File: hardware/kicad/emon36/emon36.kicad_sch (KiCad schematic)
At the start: 80 parts, among them J1 Barrel_Jack, J17 Conn_02x03_Odd_Even, J37 USB_B_Micro, J4 Barrel_Jack, SW2 SW_MEC_5E, SW3 SW_MEC_5E, SW4 SW_MEC_5E, U1 ESP32-C3-WROOM-02-N4, U11 PL133-97QC, U12 PEC12R-4117F-S0012, U3 16.384MHz, U8 TPS5403

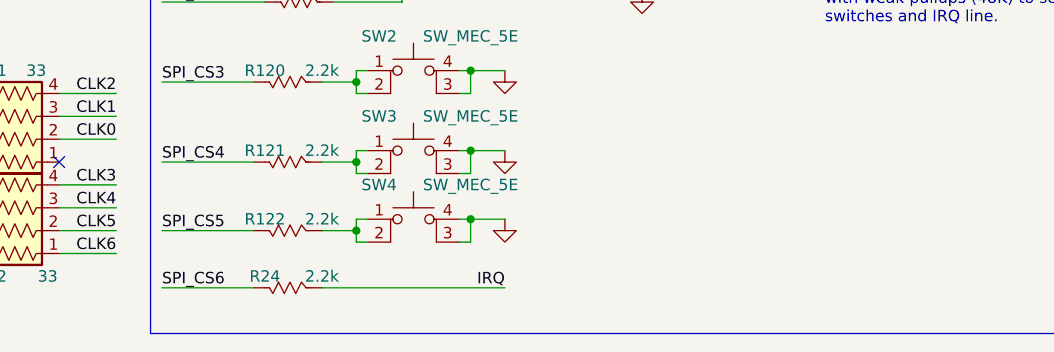
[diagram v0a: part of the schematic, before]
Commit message: Added an optional pullup resistor in case the internal one is not strong enough to boas all the IRQ diodes.
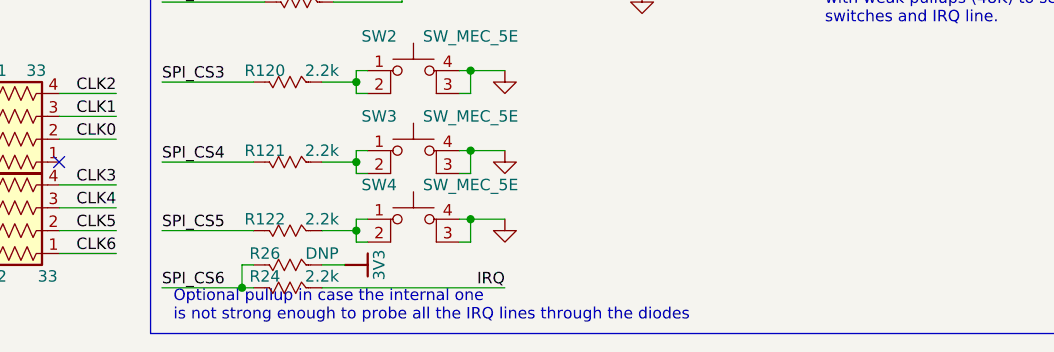
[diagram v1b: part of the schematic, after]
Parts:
- added R26: DNP, Resistor_SMD:R_0603_1608Metric, symbol emon36:R_US
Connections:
- net 3V3: now also R26.2
- net SPI_CS6: now also R26.1
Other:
- note added: "Optional pullup in case the internal one is not strong enough to probe all the IRQ lines through the diodes"
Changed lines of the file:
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@@
   (junction (at 143.51 31.75) (diameter 0) (color 0 0 0 0)
   )
+  (junction (at 119.38 199.39) (diameter 0) (color 0 0 0 0)
+  )
   (junction (at 25.4 123.19) (diameter 0) (color 0 0 0 0)
   )
@@
     (stroke (width 0) (type default) (color 0 0 0 0))
   )
-  (wire (pts (xy 110.49 199.39) (xy 120.65 199.39))
+  (wire (pts (xy 110.49 199.39) (xy 119.38 199.39))
     (stroke (width 0) (type default) (color 0 0 0 0))
   )
@@
     (stroke (width 0) (type default) (color 0 0 0 0))
   )
+  (wire (pts (xy 119.38 199.39) (xy 120.65 199.39))
+    (stroke (width 0) (type default) (color 0 0 0 0))
+  )
   (wire (pts (xy 21.59 83.82) (xy 38.1 83.82))
     (stroke (width 0) (type default) (color 0 0 0 0))
@@
     (stroke (width 0) (type default) (color 0 0 0 0))
   )
+  (wire (pts (xy 119.38 196.85) (xy 119.38 199.39))
+    (stroke (width 0) (type default) (color 0 0 0 0))
+  )
   (wire (pts (xy 213.36 20.32) (xy 213.36 29.21))
     (stroke (width 0) (type default) (color 0 0 0 0))
@@
     (stroke (width 0) (type default) (color 0 0 0 0))
   )
+  (wire (pts (xy 120.65 196.85) (xy 119.38 196.85))
+    (stroke (width 0) (type default) (color 0 0 0 0))
+  )
   (wire (pts (xy 205.74 120.65) (xy 205.74 127))
     (stroke (width 0) (type default) (color 0 0 0 0))
@@
     (stroke (width 0) (type default) (color 0 0 0 0))
   )
+  (wire (pts (xy 128.27 196.85) (xy 130.81 196.85))
+    (stroke (width 0) (type default) (color 0 0 0 0))
+  )
   (wire (pts (xy 143.51 175.26) (xy 144.78 175.26))
     (stroke (width 0) (type default) (color 0 0 0 0))
@@
     (effects (font (size 1.27 1.27)) (justify left bottom))
   )
+  (text "Optional pullup in case the internal one\nis not strong enough to probe all the IRQ lines through the diodes"
+    (at 111.76 203.2 0)
+    (effects (font (size 1.27 1.27)) (justify left bottom))
+  )
   (text "OLED Color Display\n96x64 pixels, 16-bit color\n3.3V supply, SPI interface\n"
     (at 104.14 49.53 0)
@@
     (pin "C")
   )
+  (symbol (lib_id "Top-altium-import:3V3") (at 130.81 196.85 90) (unit 1)
+    (in_bom yes) (on_board yes)
+    (property "Reference" "#PWR0111" (id 0) (at 130.81 196.85 0)
+      (effects (font (size 1.27 1.27)) hide)
+    )
+    (property "Value" "3V3" (id 1) (at 134.62 196.85 0))
+    (property "Footprint" "" (id 2) (at 130.81 196.85 0)
+      (effects (font (size 1.27 1.27)) hide)
+    )
+    (property "Datasheet" "" (id 3) (at 130.81 196.85 0)
+      (effects (font (size 1.27 1.27)) hide)
+    )
+    (pin "")
+  )
   (symbol (lib_id "Diode:B240") (at 184.15 110.49 180) (unit 1)
     (in_bom yes) (on_board yes) (fields_autoplaced)
@@
     (pin "1")
   )
+  (symbol (lib_id "emon36:R_US") (at 124.46 196.85 90) (unit 1)
+    (in_bom yes) (on_board yes)
+    (property "Reference" "R26" (id 0) (at 121.92 195.58 90))
+    (property "Value" "DNP" (id 1) (at 128.27 195.58 90))
+    (property "Footprint" "Resistor_SMD:R_0603_1608Metric" (id 2) (at 124.46 188.722 90)
+      (effects (font (size 1.27 1.27)) hide)
+    )
+    (property "Datasheet" "~" (id 3) (at 121.92 190.754 0)
+      (effects (font (size 1.27 1.27)) hide)
+    )
+    (pin "1")
+    (pin "2")
+  )
   (symbol (lib_id "Device:C_Small") (at 201.93 129.54 0) (unit 1)
     (in_bom yes) (on_board yes)
@@
       (reference "#PWR0110") (unit 1) (value "GND") (footprint "")
     )
+    (path "/1f6575e3-1ea0-4495-9f12-1278c361a28e"
+      (reference "#PWR0111") (unit 1) (value "3V3") (footprint "")
+    )
     (path "/9cd56890-7d28-4c87-8f1e-527ff584d764"
       (reference "#PWR0114") (unit 1) (value "GND") (footprint "")
@@
       (reference "R25") (unit 1) (value "21.5K") (footprint "Resistor_SMD:R_0603_1608Metric")
     )
+    (path "/d64831ce-999d-4518-9cdd-185e880b9eaa"
+      (reference "R26") (unit 1) (value "DNP") (footprint "Resistor_SMD:R_0603_1608Metric")
+    )
     (path "/8da62263-1d88-4a7c-a52f-9ab439191384"

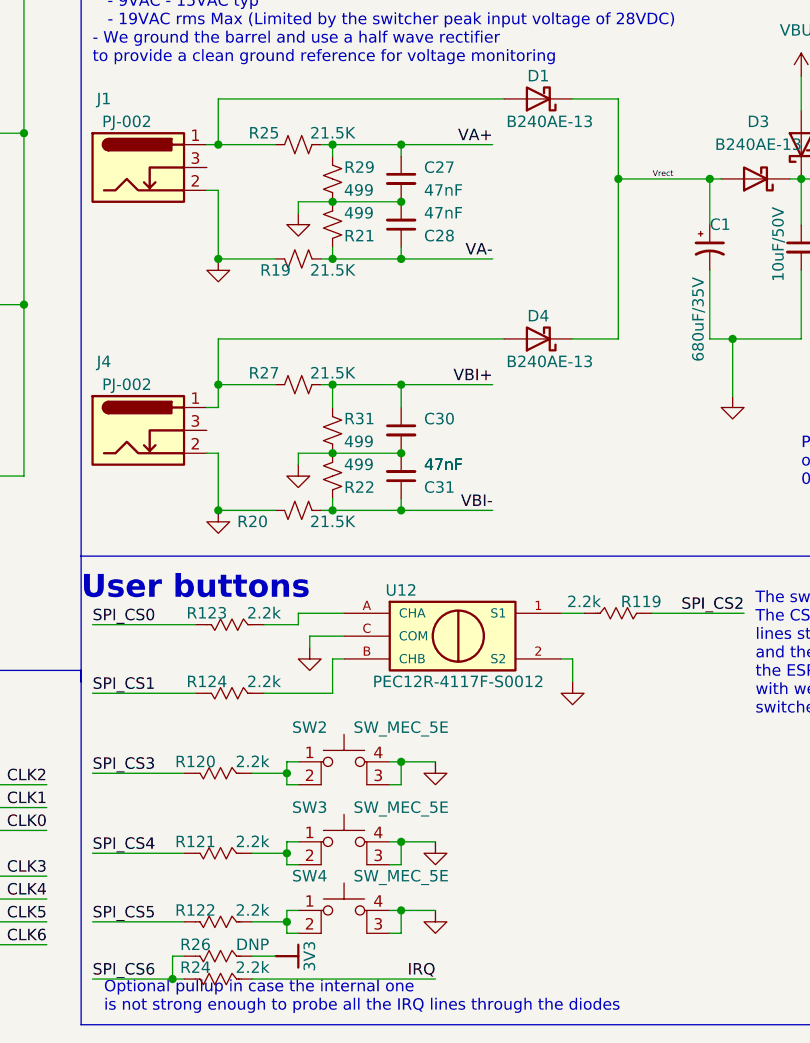
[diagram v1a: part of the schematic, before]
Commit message: Added diodes on IRQ, included solder mask and silk constraints, fix silk. Version sent to production.
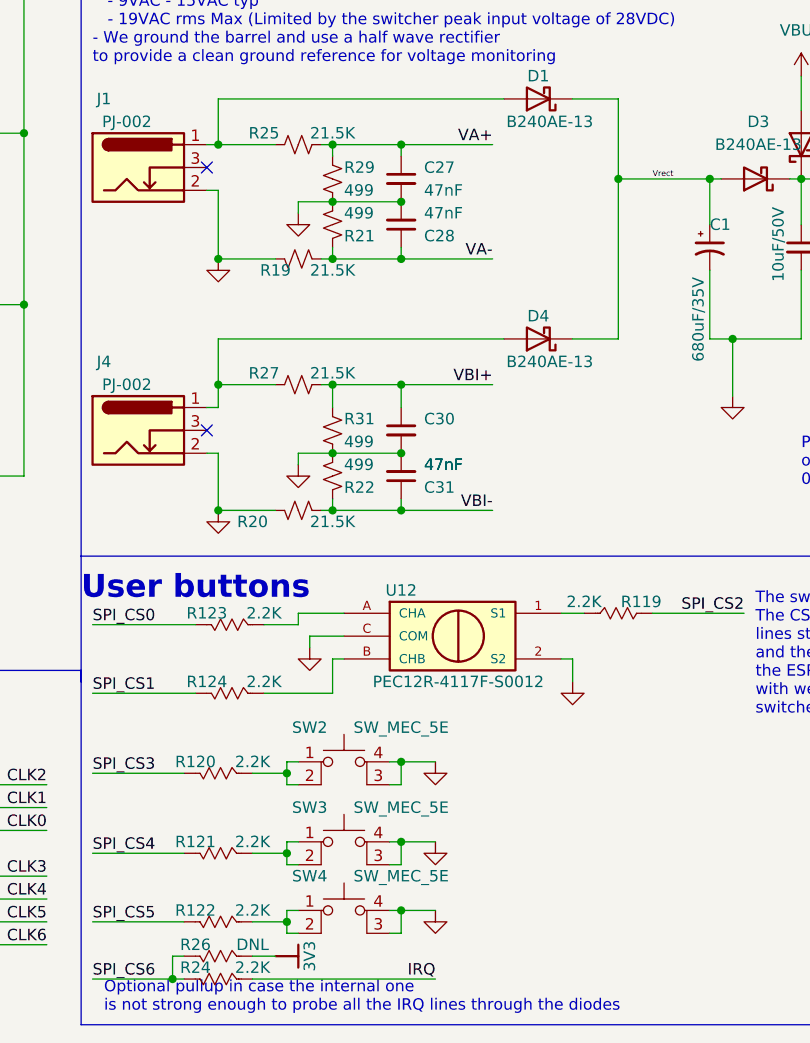
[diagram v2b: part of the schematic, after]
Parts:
- C1: Desc (none) -> CAP ALUM 680UF 20% 35V RADIAL
- C124, C21, C25, C29: Desc (none) -> CAP CER 0.22UF 25V X7R 0603; MFR (none) -> Samsung Electro-Mechanics; MPN (none) -> CL10B224KA8NNNC
- C18, C33, C6: Desc (none) -> CAP CER 0.1UF 50V X7R 0603; MFR (none) -> KYOCERA AVX; MPN (none) -> 06035C104KAT2A
- C23, C26: Desc (none) -> CAP CER 100PF 50V C0G/NP0 0603; MFR (none) -> Samsung Electro-Mechanics; MPN (none) -> CL10C101JB8NNNC
- C27, C28, C30, C31: Desc (none) -> CAP CER 0.047UF 50V X7R 0603; MFR (none) -> Samsung Electro-Mechanics; MPN (none) -> CL10B473KB8NNNC
- C4, C5: Desc (none) -> CAP CER 2200PF 50V X7R 0603; MFR (none) -> Samsung Electro-Mechanics; MPN (none) -> CL10B222KB8NFNC
- C7: Desc (none) -> CAP ALUM 220UF 20% 35V RADIAL
- C98, C99: Desc (none) -> CAP CER 22PF 16V NP0 0603; MFR (none) -> KYOCERA AVX; MPN (none) -> 0603YA220KAT2A
- D1, D2, D3, D4, D5: Desc (none) -> DIODE SCHOTTKY 40V 2A SMA; MFR Diodes Inc -> Diodes Incorporated
- DISP1: footprint emon36:SSD1331_RGB_OLED_96x64 -> emon36DIODE ARRAY SCHOTTKY 30V SOT323; Desc (none) -> OLED DISP 0.96IN 96x64 RGB SSD1331; MFR (none) -> AliExpress
- J1, J4: Desc (none) -> CONN PWR JACK 2X5.5MM SOLDER
- R119, R120, R121, R122, R123, R124, R24: value 2.2k -> 2.2K
- R26: value DNP -> DNL
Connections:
- no-connect marks 8 -> 10
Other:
- title: EMON36 - 36-channel single-board energy monitor -> EEMON42 - 36-channel single-board energy monitor
